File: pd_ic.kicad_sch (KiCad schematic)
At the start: 11 parts, among them J11 Conn_01x02, Q1 IRF9540N, U1 CYPD3175-24LQXQ

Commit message: idk it showed question marks again
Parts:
- renumbered C68 to C1, C65 to C2, C78 to C3, C71 to C4, J11 to J1, R44 to R1, R45 to R2, R46 to R3, R47 to R4
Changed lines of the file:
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@@
 		(on_board yes)
 		(dnp no)
-		(property "Reference" "J11"
+		(property "Reference" "J1"
 			(at 77.724 87.63 0)
 			(effects
@@
 		)
 		(instances
+			(project "pd_ic"
+				(path "/165a9535-5a15-47cd-8c5a-8614e72462ca"
+					(reference "J1")
+					(unit 1)
+				)
+			)
 			(project ""
 				(path "/2f56b371-1597-47e1-a48d-b7f69d342f77/a0987cd4-dfa7-4cf4-a9f1-5b392786bba7"
@@
 		(on_board yes)
 		(dnp no)
-		(property "Reference" "C68"
+		(property "Reference" "C1"
 			(at 29.21 62.2299 0)
 			(effects
@@
 		(dnp no)
 		(fields_autoplaced yes)
-		(property "Reference" "C71"
+		(property "Reference" "C4"
 			(at 69.85 93.9799 0)
 			(effects
@@
 		)
 		(instances
+			(project "pd_ic"
+				(path "/165a9535-5a15-47cd-8c5a-8614e72462ca"
+					(reference "C4")
+					(unit 1)
+				)
+			)
 			(project ""
 				(path "/2f56b371-1597-47e1-a48d-b7f69d342f77/a0987cd4-dfa7-4cf4-a9f1-5b392786bba7"
@@
 		(dnp no)
 		(fields_autoplaced yes)
-		(property "Reference" "#PWR064"
+		(property "Reference" "#PWR04"
 			(at 54.61 95.25 0)
 			(effects
@@
 		)
 		(instances
+			(project "pd_ic"
+				(path "/165a9535-5a15-47cd-8c5a-8614e72462ca"
+					(reference "#PWR04")
+					(unit 1)
+				)
+			)
 			(project ""
 				(path "/2f56b371-1597-47e1-a48d-b7f69d342f77/a0987cd4-dfa7-4cf4-a9f1-5b392786bba7"
@@
 		(dnp no)
 		(fields_autoplaced yes)
-		(property "Reference" "C65"
+		(property "Reference" "C2"
 			(at 38.1 64.7699 0)
 			(effects
@@
 		(dnp no)
 		(fields_autoplaced yes)
-		(property "Reference" "#PWR062"
+		(property "Reference" "#PWR01"
 			(at 25.4 74.93 0)
 			(effects
@@
 		(dnp no)
 		(fields_autoplaced yes)
-		(property "Reference" "R44"
+		(property "Reference" "R1"
 			(at 57.15 72.3899 0)
 			(effects
@@
 		)
 		(instances
+			(project "pd_ic"
+				(path "/165a9535-5a15-47cd-8c5a-8614e72462ca"
+					(reference "R1")
+					(unit 1)
+				)
+			)
 			(project ""
 				(path "/2f56b371-1597-47e1-a48d-b7f69d342f77/a0987cd4-dfa7-4cf4-a9f1-5b392786bba7"
@@
 		(dnp no)
 		(fields_autoplaced yes)
-		(property "Reference" "#PWR063"
+		(property "Reference" "#PWR02"
 			(at 34.29 77.47 0)
 			(effects
@@
 		(dnp no)
 		(fields_autoplaced yes)
-		(property "Reference" "#PWR065"
+		(property "Reference" "#PWR05"
 			(at 66.04 105.41 0)
 			(effects
@@
 		)
 		(instances
+			(project "pd_ic"
+				(path "/165a9535-5a15-47cd-8c5a-8614e72462ca"
+					(reference "#PWR05")
+					(unit 1)
+				)
+			)
 			(project ""
 				(path "/2f56b371-1597-47e1-a48d-b7f69d342f77/a0987cd4-dfa7-4cf4-a9f1-5b392786bba7"
@@
 		(dnp no)
 		(fields_autoplaced yes)
-		(property "Reference" "R45"
+		(property "Reference" "R2"
 			(at 57.15 82.5499 0)
 			(effects
@@
 		)
 		(instances
+			(project "pd_ic"
+				(path "/165a9535-5a15-47cd-8c5a-8614e72462ca"
+					(reference "R2")
+					(unit 1)
+				)
+			)
 			(project ""
 				(path "/2f56b371-1597-47e1-a48d-b7f69d342f77/a0987cd4-dfa7-4cf4-a9f1-5b392786bba7"
@@
 		(dnp no)
 		(fields_autoplaced yes)
-		(property "Reference" "R47"
+		(property "Reference" "R4"
 			(at 111.76 125.73 90)
 			(effects
@@
 		)
 		(instances
+			(project "pd_ic"
+				(path "/165a9535-5a15-47cd-8c5a-8614e72462ca"
+					(reference "R4")
+					(unit 1)
+				)
+			)
 			(project ""
 				(path "/2f56b371-1597-47e1-a48d-b7f69d342f77/a0987cd4-dfa7-4cf4-a9f1-5b392786bba7"
@@
 		(dnp no)
 		(fields_autoplaced yes)
-		(property "Reference" "#PWR061"
+		(property "Reference" "#PWR03"
 			(at 104.14 140.97 0)
 			(effects
@@
 		(dnp no)
 		(fields_autoplaced yes)
-		(property "Reference" "R46"
+		(property "Reference" "R3"
 			(at 68.58 85.0899 0)
 			(effects
@@
 		)
 		(instances
+			(project "pd_ic"
+				(path "/165a9535-5a15-47cd-8c5a-8614e72462ca"
+					(reference "R3")
+					(unit 1)
+				)
+			)
 			(project ""
 				(path "/2f56b371-1597-47e1-a48d-b7f69d342f77/a0987cd4-dfa7-4cf4-a9f1-5b392786bba7"
@@
 		(on_board yes)
 		(dnp no)
-		(property "Reference" "C78"
+		(property "Reference" "C3"
 			(at 19.05 62.2299 0)
 			(effects
@@
 		)
 		(instances
+			(project "pd_ic"
+				(path "/165a9535-5a15-47cd-8c5a-8614e72462ca"
+					(reference "C3")
+					(unit 1)
+				)
+			)
 			(project "robot_pcb"
 				(path "/2f56b371-1597-47e1-a48d-b7f69d342f77/a0987cd4-dfa7-4cf4-a9f1-5b392786bba7"
@@
 		)
 	)
+	(sheet_instances
+		(path "/"
+			(page "1")
+		)
+	)
+	(embedded_fonts no)
 )

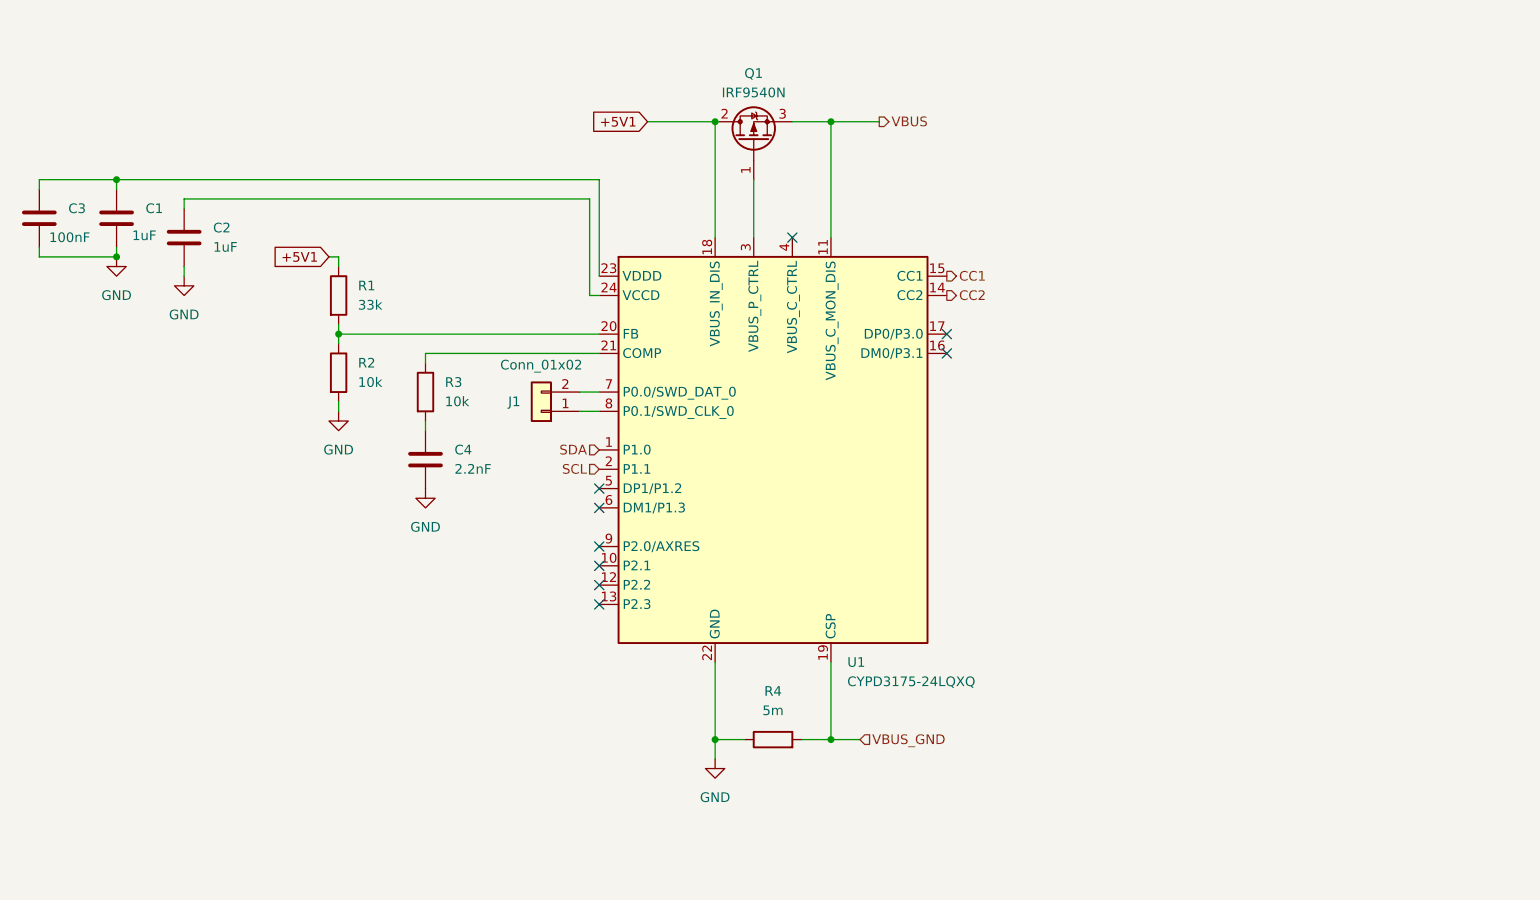
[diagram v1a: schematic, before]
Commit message: mounting holes for handle + updated pcb from sch
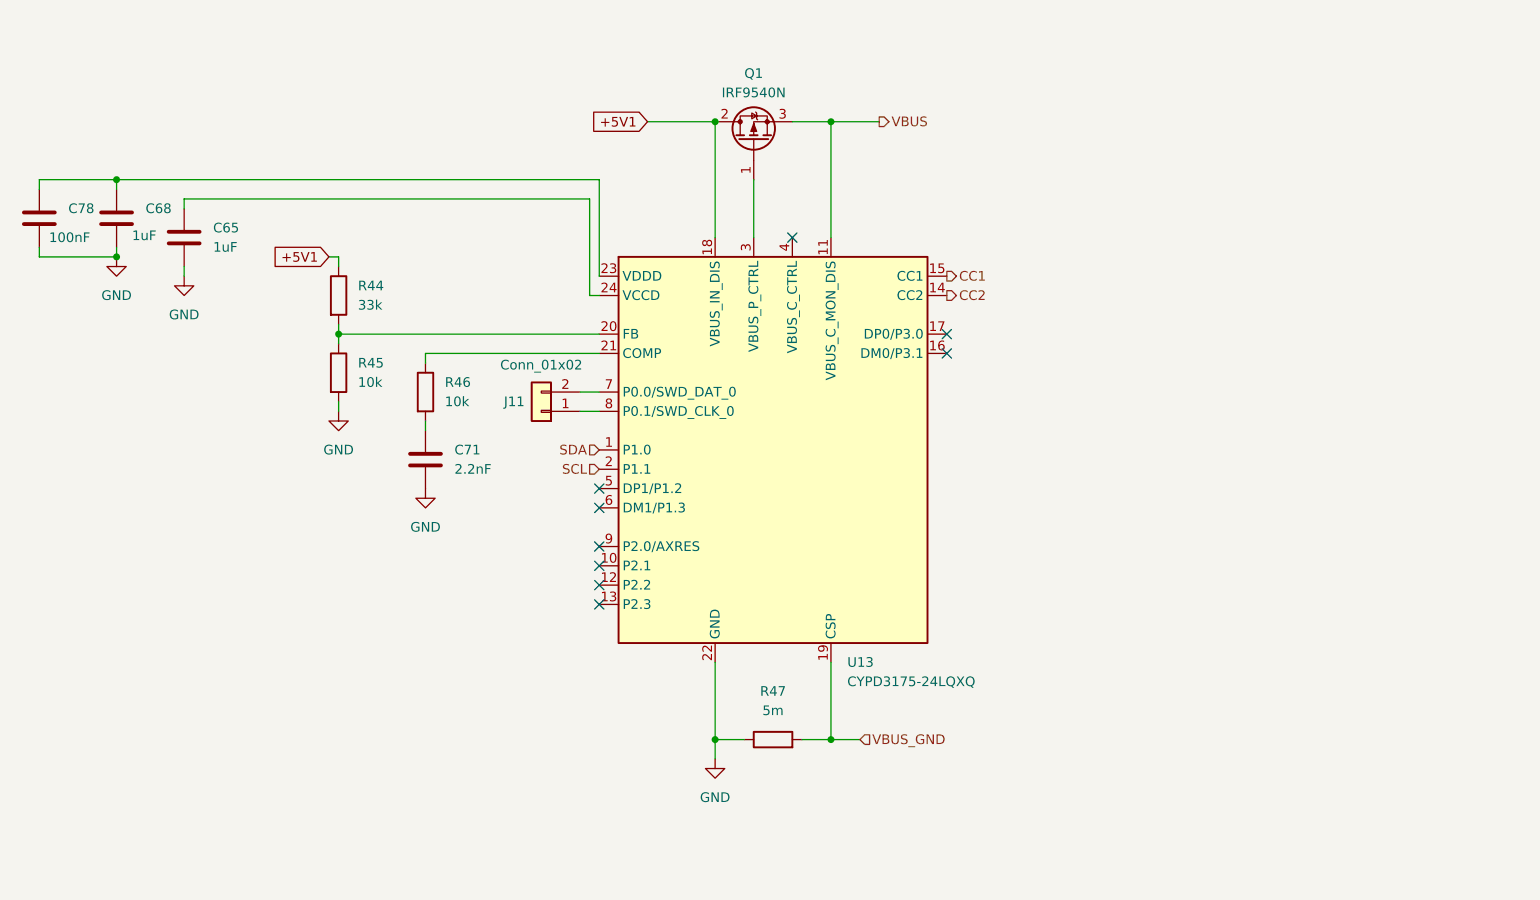
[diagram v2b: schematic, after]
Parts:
- renumbered C2 to C65, C1 to C68, C4 to C71, C3 to C78, J1 to J11, R1 to R44, R2 to R45, R3 to R46, R4 to R47, U1 to U13
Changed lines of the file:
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@@
 		(on_board yes)
 		(dnp no)
-		(property "Reference" "J1"
+		(property "Reference" "J11"
 			(at 77.724 87.63 0)
 			(effects
@@
 		(on_board yes)
 		(dnp no)
-		(property "Reference" "C1"
+		(property "Reference" "C68"
 			(at 29.21 62.2299 0)
 			(effects
@@
 		(dnp no)
 		(fields_autoplaced yes)
-		(property "Reference" "C4"
+		(property "Reference" "C71"
 			(at 69.85 93.9799 0)
 			(effects
@@
 		(dnp no)
 		(fields_autoplaced yes)
-		(property "Reference" "#PWR04"
+		(property "Reference" "#PWR064"
 			(at 54.61 95.25 0)
 			(effects
@@
 		(dnp no)
 		(fields_autoplaced yes)
-		(property "Reference" "C2"
+		(property "Reference" "C65"
 			(at 38.1 64.7699 0)
 			(effects
@@
 		(dnp no)
 		(fields_autoplaced yes)
-		(property "Reference" "#PWR01"
+		(property "Reference" "#PWR062"
 			(at 25.4 74.93 0)
 			(effects
@@
 		(dnp no)
 		(fields_autoplaced yes)
-		(property "Reference" "U1"
+		(property "Reference" "U13"
 			(at 121.5233 121.92 0)
 			(effects
@@
 		(dnp no)
 		(fields_autoplaced yes)
-		(property "Reference" "R1"
+		(property "Reference" "R44"
 			(at 57.15 72.3899 0)
 			(effects
@@
 		(dnp no)
 		(fields_autoplaced yes)
-		(property "Reference" "#PWR02"
+		(property "Reference" "#PWR063"
 			(at 34.29 77.47 0)
 			(effects
@@
 		(dnp no)
 		(fields_autoplaced yes)
-		(property "Reference" "#PWR05"
+		(property "Reference" "#PWR065"
 			(at 66.04 105.41 0)
 			(effects
@@
 		(dnp no)
 		(fields_autoplaced yes)
-		(property "Reference" "R2"
+		(property "Reference" "R45"
 			(at 57.15 82.5499 0)
 			(effects
@@
 		(dnp no)
 		(fields_autoplaced yes)
-		(property "Reference" "R4"
+		(property "Reference" "R47"
 			(at 111.76 125.73 90)
 			(effects
@@
 		(dnp no)
 		(fields_autoplaced yes)
-		(property "Reference" "#PWR03"
+		(property "Reference" "#PWR061"
 			(at 104.14 140.97 0)
 			(effects
@@
 		(dnp no)
 		(fields_autoplaced yes)
-		(property "Reference" "R3"
+		(property "Reference" "R46"
 			(at 68.58 85.0899 0)
 			(effects
@@
 		(on_board yes)
 		(dnp no)
-		(property "Reference" "C3"
+		(property "Reference" "C78"
 			(at 19.05 62.2299 0)
 			(effects

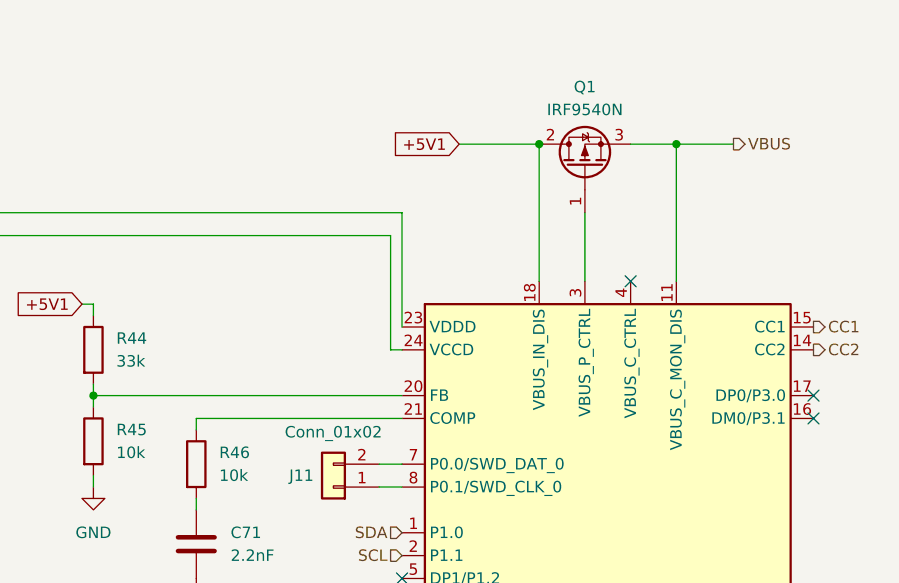
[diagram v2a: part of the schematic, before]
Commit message: added usb c thing to pcb
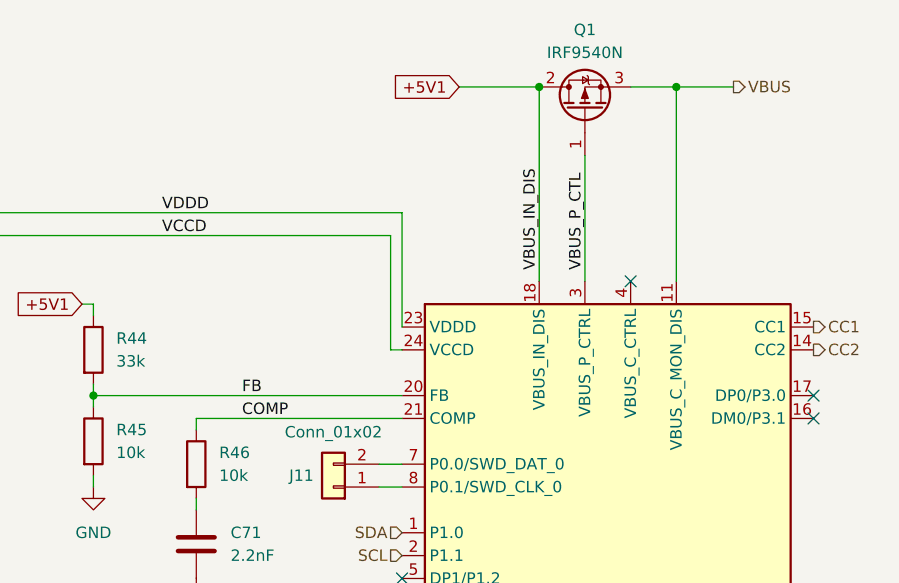
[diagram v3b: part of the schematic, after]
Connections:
- net VDDD: now reaches C68.1, C78.1, U13.23 (VDDD)
- net VCCD: now reaches C65.1, U13.24 (VCCD)
- net FB: now reaches R44.2, R45.1, U13.20 (FB)
- net COMP: now reaches R46.1, U13.21 (COMP)
- net VBUS_P_CTL: now reaches Q1.1 (G), U13.3 (VBUS_P_CTRL)
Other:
- moved on the sheet: Q1
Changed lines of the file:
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@@
 	)
 	(junction
-		(at 104.14 50.8)
+		(at 104.14 44.45)
 		(diameter 0)
 		(color 0 0 0 0)
 	)
 	(junction
-		(at 119.38 50.8)
+		(at 119.38 44.45)
 		(diameter 0)
 		(color 0 0 0 0)
@@
 	(wire
 		(pts
-			(xy 109.22 58.42) (xy 109.22 66.04)
+			(xy 109.22 52.07) (xy 109.22 66.04)
 		)
 		(stroke
@@
 	(wire
 		(pts
-			(xy 114.3 50.8) (xy 119.38 50.8)
+			(xy 114.3 44.45) (xy 119.38 44.45)
 		)
 		(stroke
@@
 	(wire
 		(pts
-			(xy 95.25 50.8) (xy 104.14 50.8)
+			(xy 95.25 44.45) (xy 104.14 44.45)
 		)
 		(stroke
@@
 	(wire
 		(pts
-			(xy 104.14 50.8) (xy 104.14 66.04)
-		)
-		(stroke
-			(width 0)
-			(type default)
-		)
-	)
-	(wire
-		(pts
 			(xy 104.14 132.08) (xy 107.95 132.08)
 		)
@@
 	(wire
 		(pts
+			(xy 119.38 44.45) (xy 119.38 66.04)
+		)
+		(stroke
+			(width 0)
+			(type default)
+		)
+	)
+	(wire
+		(pts
 			(xy 88.9 58.42) (xy 88.9 71.12)
 		)
@@
 	(wire
 		(pts
+			(xy 104.14 44.45) (xy 104.14 66.04)
+		)
+		(stroke
+			(width 0)
+			(type default)
+		)
+	)
+	(wire
+		(pts
 			(xy 53.34 68.58) (xy 54.61 68.58)
 		)
@@
 	(wire
 		(pts
-			(xy 119.38 50.8) (xy 125.73 50.8)
+			(xy 119.38 44.45) (xy 125.73 44.45)
 		)
 		(stroke
@@
 		)
 	)
-	(wire
-		(pts
-			(xy 119.38 50.8) (xy 119.38 66.04)
-		)
-		(stroke
-			(width 0)
-			(type default)
+	(label "VDDD"
+		(at 62.23 58.42 0)
+		(effects
+			(font
+				(size 1.27 1.27)
+			)
+			(justify left bottom)
+		)
+	)
+	(label "VBUS_P_CTL"
+		(at 109.22 64.77 90)
+		(effects
+			(font
+				(size 1.27 1.27)
+			)
+			(justify left bottom)
+		)
+	)
+	(label "FB"
+		(at 71.12 78.74 0)
+		(effects
+			(font
+				(size 1.27 1.27)
+			)
+			(justify left bottom)
+		)
+	)
+	(label "COMP"
+		(at 71.12 81.28 0)
+		(effects
+			(font
+				(size 1.27 1.27)
+			)
+			(justify left bottom)
+		)
+	)
+	(label "VCCD"
+		(at 62.23 60.96 0)
+		(effects
+			(font
+				(size 1.27 1.27)
+			)
+			(justify left bottom)
+		)
+	)
+	(label "VBUS_IN_DIS"
+		(at 104.14 64.77 90)
+		(effects
+			(font
+				(size 1.27 1.27)
+			)
+			(justify left bottom)
 		)
 	)
 	(global_label "+5V1"
 		(shape input)
-		(at 95.25 50.8 180)
+		(at 95.25 44.45 180)
 		(fields_autoplaced yes)
 		(effects
@@
 		)
 		(property "Intersheetrefs" "${INTERSHEET_REFS}"
-			(at 87.1848 50.8 0)
+			(at 87.1848 44.45 0)
 			(effects
 				(font
@@
 	(hierarchical_label "VBUS"
 		(shape output)
-		(at 125.73 50.8 0)
+		(at 125.73 44.45 0)
 		(effects
 			(font
@@
 	(symbol
 		(lib_id "Transistor_FET:IRF9540N")
-		(at 109.22 53.34 90)
+		(at 109.22 46.99 90)
 		(unit 1)
 		(exclude_from_sim no)
@@
 		(fields_autoplaced yes)
 		(property "Reference" "Q1"
-			(at 109.22 44.45 90)
+			(at 109.22 38.1 90)
 			(effects
 				(font
@@
 		)
 		(property "Value" "IRF9540N"
-			(at 109.22 46.99 90)
+			(at 109.22 40.64 90)
 			(effects
 				(font
@@
 		)
 		(property "Footprint" "Package_TO_SOT_THT:TO-220-3_Horizontal_TabDown"
-			(at 111.125 48.26 0)
+			(at 111.125 41.91 0)
 			(effects
 				(font
@@
 		)
 		(property "Datasheet" "http://www.irf.com/product-info/datasheets/data/irf9540n.pdf"
-			(at 113.03 48.26 0)
+			(at 113.03 41.91 0)
 			(effects
 				(font
@@
 		)
 		(property "Description" "-23A Id, -100V Vds, 117mOhm Rds, P-Channel HEXFET Power MOSFET, TO-220"
-			(at 109.22 53.34 0)
-			(effects
-				(font
+			(at 109.22 46.99 0)
+			(effects
+				(font

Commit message: hopefully those can be left as nc unless google ai is gaslighting me
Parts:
- removed C71: 2.2nF, Capacitor_SMD:C_0402_1005Metric, symbol Device:C
- removed R44: 33k, Resistor_SMD:R_0402_1005Metric, symbol Device:R
- removed R45, R46: 10k, Resistor_SMD:R_0402_1005Metric, symbol Device:R
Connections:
- net GND: no longer C68.2, C78.2
- net VDDD: no longer C68.1, C78.1
- net COMP: no longer names the net of U13.21 (COMP)
- net FB: no longer names the net of U13.20 (FB)
- no-connect marks 9 -> 11
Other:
- moved on the sheet: C68, C78

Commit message: huhhhhh
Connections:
- net GND: now also C68.2, C78.2
- net VDDD: now also C68.1, C78.1
- no-connect marks 11 -> 9
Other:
- moved on the sheet: C68, C78
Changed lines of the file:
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@@
-	)
-	(no_connect
-		(at 88.9 81.28)
 	)
 	(no_connect
@@
 	(no_connect
 		(at 88.9 111.76)
-	)
-	(no_connect
-		(at 88.9 78.74)
 	)
 	(no_connect
@@
 	(symbol
 		(lib_id "Device:C")
-		(at 20.32 63.5 0)
-		(mirror y)
+		(at 25.4 63.5 0)
 		(unit 1)
 		(exclude_from_sim no)
@@
 		(dnp no)
 		(property "Reference" "C68"
-			(at 16.51 62.2299 0)
+			(at 29.21 62.2299 0)
 			(effects
 				(font
@@
 		)
 		(property "Value" "1uF"
-			(at 18.288 65.786 0)
+			(at 27.432 65.786 0)
 			(effects
 				(font
@@
 		)
 		(property "Footprint" "Capacitor_SMD:C_0402_1005Metric"
-			(at 19.3548 67.31 0)
+			(at 26.3652 67.31 0)
 			(effects
 				(font
@@
 		)
 		(property "Datasheet" "~"
-			(at 20.32 63.5 0)
+			(at 25.4 63.5 0)
 			(effects
 				(font
@@
 		)
 		(property "Description" "Unpolarized capacitor"
-			(at 20.32 63.5 0)
+			(at 25.4 63.5 0)
 			(effects
 				(font
@@
 	(symbol
 		(lib_id "Device:C")
-		(at 30.48 63.5 0)
-		(mirror y)
+		(at 15.24 63.5 0)
 		(unit 1)
 		(exclude_from_sim no)
@@
 		(dnp no)
 		(property "Reference" "C78"
-			(at 26.67 62.2299 0)
+			(at 19.05 62.2299 0)
 			(effects
 				(font
@@
 		)
 		(property "Value" "100nF"
-			(at 29.21 66.04 0)
+			(at 16.51 66.04 0)
 			(effects
 				(font
@@
 		)
 		(property "Footprint" "Capacitor_SMD:C_0402_1005Metric"
-			(at 29.5148 67.31 0)
+			(at 16.2052 67.31 0)
 			(effects
 				(font
@@
 		)
 		(property "Datasheet" "~"
-			(at 30.48 63.5 0)
+			(at 15.24 63.5 0)
 			(effects
 				(font
@@
 		)
 		(property "Description" "Unpolarized capacitor"
-			(at 30.48 63.5 0)
-			(effects
-				(font
+			(at 15.24 63.5 0)
+			(effects
+				(font
